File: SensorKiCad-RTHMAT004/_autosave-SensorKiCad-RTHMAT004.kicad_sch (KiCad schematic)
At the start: 19 parts, among them J1 Conn_02x14_Odd_Even, Q1 SS8050

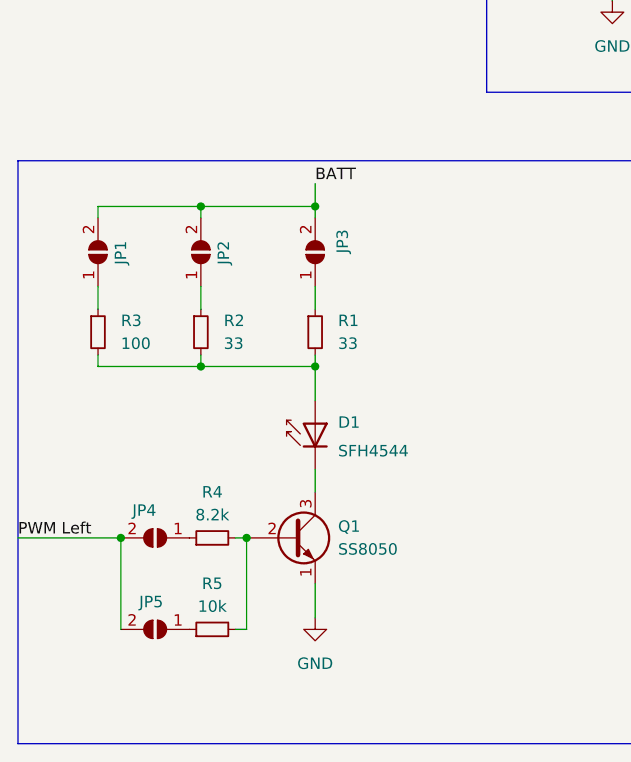
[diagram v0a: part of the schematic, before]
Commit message: Small changes to Sensor KiCAD file
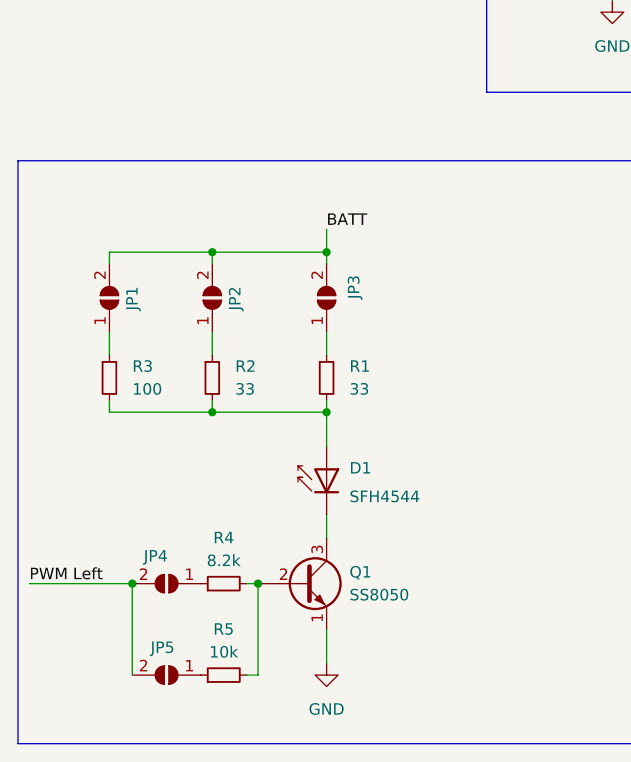
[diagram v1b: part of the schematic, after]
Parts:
- R1: footprint Resistor_SMD:R_0815_2038Metric -> Resistor_SMD:R_0805_2012Metric
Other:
- moved on the sheet: D1, JP1, JP2, JP3, JP4, JP5, Q1, R1, R2, R3, R4, R5
